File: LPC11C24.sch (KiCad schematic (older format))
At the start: 18 parts

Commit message: changed the controller adding some shift registers
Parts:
- added C18, C24: C, ~, symbol C
- added C21, C26: C, 10nF, symbol C
- added D30, D31: ZENER, ~, symbol ZENER
- added HB1: LED, ~, symbol LED
- added P12: CONN_6, symbol CONN_6
- added P14: JTAG, symbol CONN_5X2
- added R50, R51, R56, R57, R61: R, ~, symbol R
- added RP? (x2): R_PACK8, ~, symbol R_PACK8
- added U10, U11: 74LS165, ~, symbol 74LS165
- added U9: 74LS595, ~, symbol 74LS595
- C25: renamed from C?; value C -> 1nF
- R58: renamed from R?; footprint 10k -> 12k
- X1: renamed from X?; value CRYSTAL -> 12MHz
- gave numbers to parts that had none: 15
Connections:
- net labels added: +12V, 12V_SENSE_VOLTAGE, 50V_SENSE_VOLTAGE, CTS, DATA_CLOCK, DATA_LOAD, DATA_OUT, FTDI_RXD, FTDI_TXD, FTDI_VCC, HB_LED, JTAG_RESET, JTAG_RTCK, JTAG_TCLK_SWCLK, JTAG_TDI, JTAG_TDO_SWO, JTAG_TMS_SWDIO, RTS, SOL_PWR_F
- net labels removed: ADC4, ADC6, ADC7
- wire segments 66 -> 224
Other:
- note added: "IP - 3 I/Os lamp matrix shift register\n8 I/Os switch matrix\nIP - 3 I/Os address DIP switch shift register\n8 I/Os solenoids\nDONE - 2 I/Os UART to FTDI cable 6-pin header\nIP - 1 I/O heartbeat LED\nDONE - 4 I/Os JTAG (SWCLK / SWDIO / RESET / maybe MOSI, check http://www.embeddedartists.com/sites/default/files/docs/schematics/LPCXpressoLPC11C24revB.pdf)\nDONE - 2 I/Os voltage sense ADC\nDONE - 2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"
- moved on the sheet: C27, P13, R59, R60, SW1, SW2

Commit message: finished main controller, added LED's to power system.
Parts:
- added DBG: LED, ~, symbol LED
- added R?: R, ~, symbol R
- renumbered HB1 to HB
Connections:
- net ADC5 is gone; now on net SOL_0: U8.40 (PIO1_4/AD5/CT32B1_MAT3/WAKEUP)
- net DATA_CLOCK is gone; now on net DIP_CLOCK: U10.2 (CP), U11.2 (CP)
- net DATA_LOAD is gone; now on net DIP_LOAD: U10.1 (Pl), U11.1 (Pl)
- net DATA_OUT is gone; now on net DIP_OUT: U11.9 (Q7)
- net +3.3V: now also U9.10 (SRCLR), R?.1
- net GND: now also U10.10 (Ds), U9.13 (G)
- net HB_LED: now also U8.32 (R/PIO0_11/AD0/CT32B0_MAT3), DBG.2 (K)
- net SOL_1: now also U8.45 (PIO1_5/~RTS~/CT32B0_CAP0)
- net SOL_2: now also U8.9 (PIO1_8/CT16B1_CAP0)
- net SOL_3: now also U8.31 (PIO2_11/SCK0)
- net SOL_4: now also U8.36 (PIO3_0/~DTR)
- net SOL_5: now also U8.37 (PIO3_1/~DSR)
- net SOL_6: now also U8.43 (PIO3_2/~DCD)
- net SOL_7: now also U8.48 (PIO3_3/~RI)
- net SW_COL_0: now also U8.1 (PIO2_6)
- net SW_COL_1: now also U8.11 (PIO2_7)
- net SW_COL_2: now also U8.12 (PIO2_8)
- net SW_COL_3: now also U8.25 (PIO2_10)
- net SW_ROW_0: now also U8.2 (PIO2_0/~DTR~/SSEL1)
- net SW_ROW_1: now also U8.13 (PIO2_1/~DSR~/SCK1)
- net SW_ROW_2: now also U8.26 (PIO2_2/~DCD~/MISO1)
- net SW_ROW_3: now also U8.38 (PIO2_3/~RI~/MOSI1)
- net LMP_CLK: now reaches U8.10 (PIO0_2/SSEL0/CT16B0_CAP0)
- net LMP_CLK: now also U9.11 (SRCLK)
- net LMP_OUT_LATCH: now reaches U8.14 (PIO0_3)
- net LMP_OUT_LATCH: now also U9.12 (RCLK)
- net DIP_LOAD: now reaches U8.23 (PIO0_6/SCK0)
- net DIP_CLOCK: now reaches U8.24 (PIO0_7/~CTS)
- net DIP_OUT: now reaches U8.27 (PIO0_8/MISO0/CT16B0_MAT0)
- net LMP_DAT: now reaches U8.4 (PIO0_1/CLKOUT/CT32B0_MAT2)
- net LMP_DAT: now also U9.14 (SER)
- net 50V_SENSE_VOLTAGE renamed SOL_PWR_SENSE_VOLTAGE
- net LP_COL_0 renamed LMP_COL_0
- net LP_COL_1 renamed LMP_COL_1
- net LP_COL_2 renamed LMP_COL_2
- net LP_COL_3 renamed LMP_COL_3
- net LP_ROW_0 renamed LMP_ROW_0
- net LP_ROW_1 renamed LMP_ROW_1
- net LP_ROW_2 renamed LMP_ROW_2
- net LP_ROW_3 renamed LMP_ROW_3
- new net: DBG.1 (A), R?.2
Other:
- note added: "DONE - 3 I/Os lamp matrix shift register\nDOEN - 8 I/Os switch matrix\nDONE - 3 I/Os address DIP switch shift register\nDONE - 8 I/Os solenoids\nDONE - 2 I/Os UART to FTDI cable 6-pin header\nDONE - 1 I/O heartbeat LED\nDONE - 4 I/Os JTAG (SWCLK / SWDIO / RESET / maybe MOSI, check http://www.embeddedartists.com/sites/default/files/docs/schematics/LPCXpressoLPC11C24revB.pdf)\nDONE - 2 I/Os voltage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"
- note removed: "IP - 3 I/Os lamp matrix shift register\n8 I/Os switch matrix\nIP - 3 I/Os address DIP switch shift register\n8 I/Os solenoids\nDONE - 2 I/Os UART to FTDI cable 6-pin header\nIP - 1 I/O heartbeat LED\nDONE - 4 I/Os JTAG (SWCLK / SWDIO / RESET / maybe MOSI, check http://www.embeddedartists.com/sites/default/files/docs/schematics/LPCXpressoLPC11C24revB.pdf)\nDONE - 2 I/Os voltage sense ADC\nDONE - 2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"
- moved on the sheet: C18, C24, D30, D31, HB, P14, R50, R51, R56, R57, R61, RP?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

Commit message: ran an ERC and touched up a couple small issues
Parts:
- gave numbers to parts that had none: 3
- renumbered C19 to C18, C18 to C19, C25 to C24, C26 to C25, C24 to C26, DBG to DBG1, HB to HB1, R50 to R54, R51 to R55, R52 to R56, R53 to R57, R54 to R58, R55 to R59, R58 to R60, R56 to R61, R57 to R62, R59 to R63, R60 to R64, R61 to R66
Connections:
- no-connect marks 0 -> 10
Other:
- moved on the sheet: P12

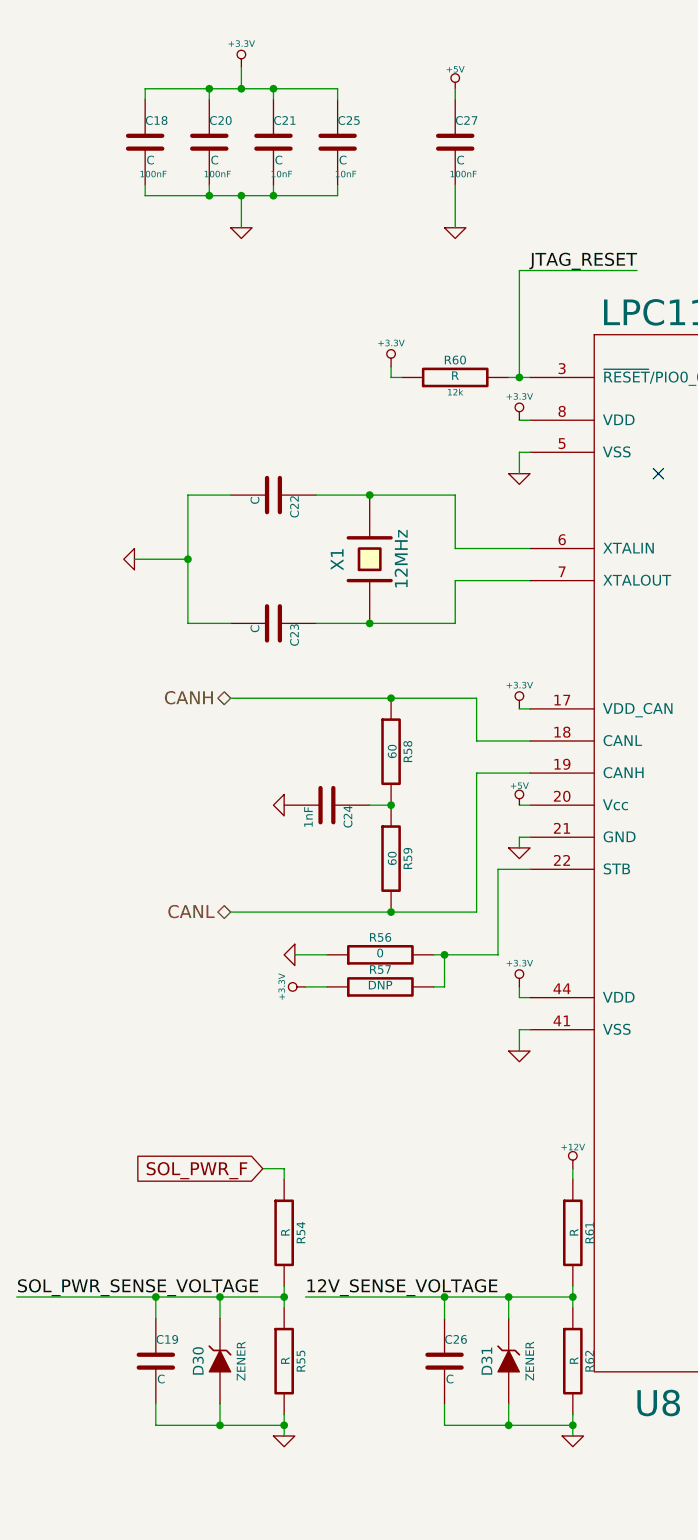
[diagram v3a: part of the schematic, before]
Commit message: added some more info to the different components, changed the pinout for zeeners, and am hating ki-cad for schematic to pads.
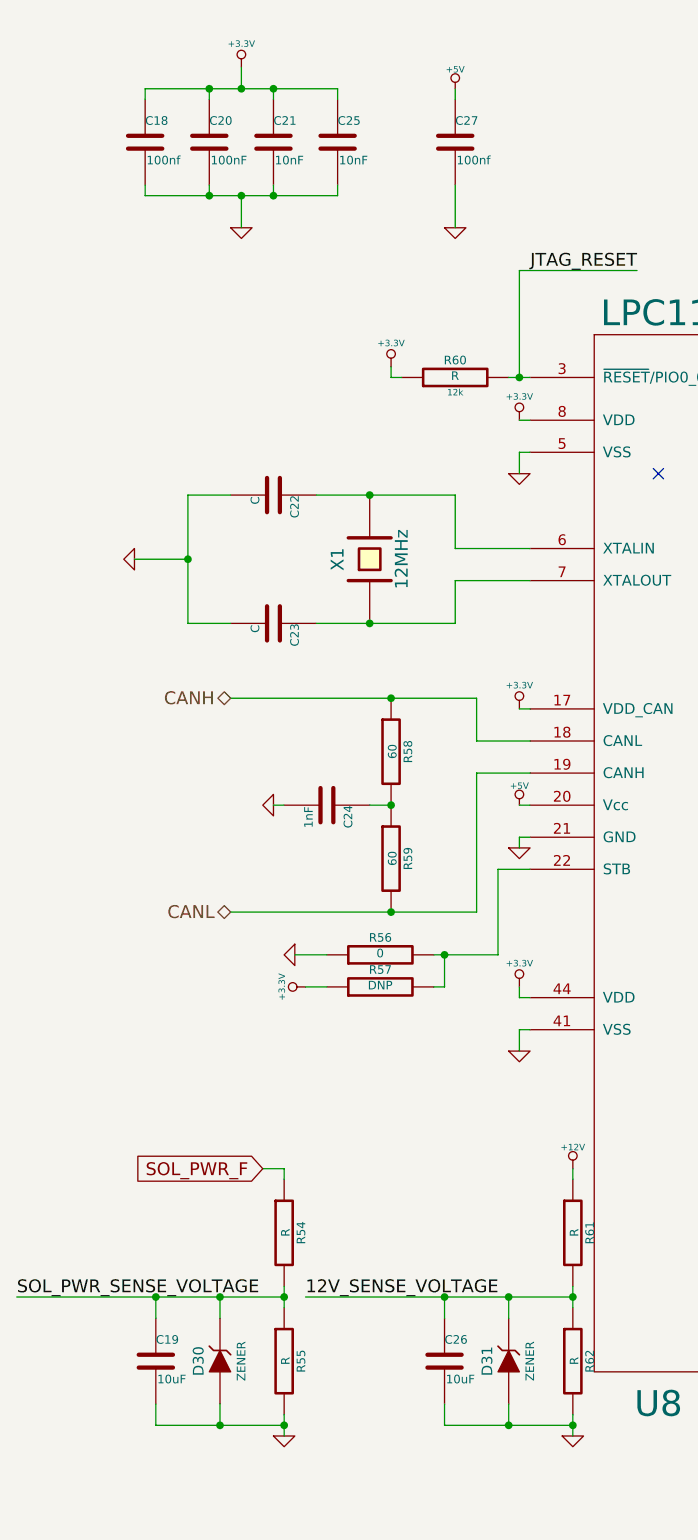
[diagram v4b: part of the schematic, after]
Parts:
- C18, C27: value C -> 100nf; footprint 100nF -> ~
- C19, C26: value C -> 10uF
- C20: value C -> 100nF; footprint 100nF -> ~
- C21, C25: value C -> 10nF; footprint 10nF -> ~
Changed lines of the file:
@@
-EESchema Schematic File Version 2  date 4/18/2013 1:12:38 AM
+EESchema Schematic File Version 2  date 4/19/2013 12:46:09 AM
 LIBS:power
 LIBS:device
@@
 Sheet 10 10
 Title ""
-Date "18 apr 2013"
+Date "19 apr 2013"
 Rev ""
 Comp ""
@@
 P 1200 1050
 F 0 "C20" H 1200 1150 40  0000 L CNN
-F 1 "C" H 1206 965 40  0000 L CNN
-F 2 "100nF" H 1238 900 30  0000 C CNN
+F 1 "100nF" H 1206 965 40  0000 L CNN
+F 2 "~" H 1238 900 30  0000 C CNN
 F 3 "~" H 1200 1050 60  0000 C CNN
 	1    1200 1050
@@
 P 900 1050
 F 0 "C18" H 900 1150 40  0000 L CNN
-F 1 "C" H 906 965 40  0000 L CNN
-F 2 "100nF" H 938 900 30  0000 C CNN
+F 1 "100nf" H 906 965 40  0000 L CNN
+F 2 "~" H 938 900 30  0000 C CNN
 F 3 "~" H 900 1050 60  0000 C CNN
 	1    900  1050
@@
 L GND #PWR065
 U 1 1 516A7ABF
-P 1550 4150
-F 0 "#PWR065" H 1550 4150 30  0001 C CNN
-F 1 "GND" H 1550 4080 30  0001 C CNN
-F 2 "" H 1550 4150 60  0000 C CNN
-F 3 "" H 1550 4150 60  0000 C CNN
-	1    1550 4150
+P 1500 4150
+F 0 "#PWR065" H 1500 4150 30  0001 C CNN
+F 1 "GND" H 1500 4080 30  0001 C CNN
+F 2 "" H 1500 4150 60  0000 C CNN
+F 3 "" H 1500 4150 60  0000 C CNN
+	1    1500 4150
 	0    1    1    0
 $EndComp
@@
 P 2350 1050
 F 0 "C27" H 2350 1150 40  0000 L CNN
-F 1 "C" H 2356 965 40  0000 L CNN
-F 2 "100nF" H 2388 900 30  0000 C CNN
+F 1 "100nf" H 2356 965 40  0000 L CNN
+F 2 "~" H 2388 900 30  0000 C CNN
 F 3 "~" H 2350 1050 60  0000 C CNN
 	1    2350 1050
@@
 P 1800 1050
 F 0 "C25" H 1800 1150 40  0000 L CNN
-F 1 "C" H 1806 965 40  0000 L CNN
-F 2 "10nF" H 1838 900 30  0000 C CNN
+F 1 "10nF" H 1806 965 40  0000 L CNN
+F 2 "~" H 1838 900 30  0000 C CNN
 F 3 "~" H 1800 1050 60  0000 C CNN
 	1    1800 1050
@@
 P 1500 1050
 F 0 "C21" H 1500 1150 40  0000 L CNN
-F 1 "C" H 1506 965 40  0000 L CNN
-F 2 "10nF" H 1538 900 30  0000 C CNN
+F 1 "10nF" H 1506 965 40  0000 L CNN
+F 2 "~" H 1538 900 30  0000 C CNN
 F 3 "~" H 1500 1050 60  0000 C CNN
 	1    1500 1050
@@
 P 2300 6750
 F 0 "C26" H 2300 6850 40  0000 L CNN
-F 1 "C" H 2306 6665 40  0000 L CNN
+F 1 "10uF" H 2306 6665 40  0000 L CNN
 F 2 "~" H 2338 6600 30  0000 C CNN
 F 3 "~" H 2300 6750 60  0000 C CNN
@@
 P 950 6750
 F 0 "C19" H 950 6850 40  0000 L CNN
-F 1 "C" H 956 6665 40  0000 L CNN
+F 1 "10uF" H 956 6665 40  0000 L CNN
 F 2 "~" H 988 6600 30  0000 C CNN
 F 3 "~" H 950 6750 60  0000 C CNN
@@
 NoConn ~ 14450 2450
 NoConn ~ 3300 2600
+Wire Wire Line
+	1500 4150 1550 4150
 $EndSCHEMATC
